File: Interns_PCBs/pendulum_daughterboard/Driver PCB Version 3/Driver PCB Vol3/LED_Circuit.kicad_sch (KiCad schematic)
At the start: 38 parts, among them J4 Conn_01x04, U1 4081, U2 4011, U3 4011, U4 4071

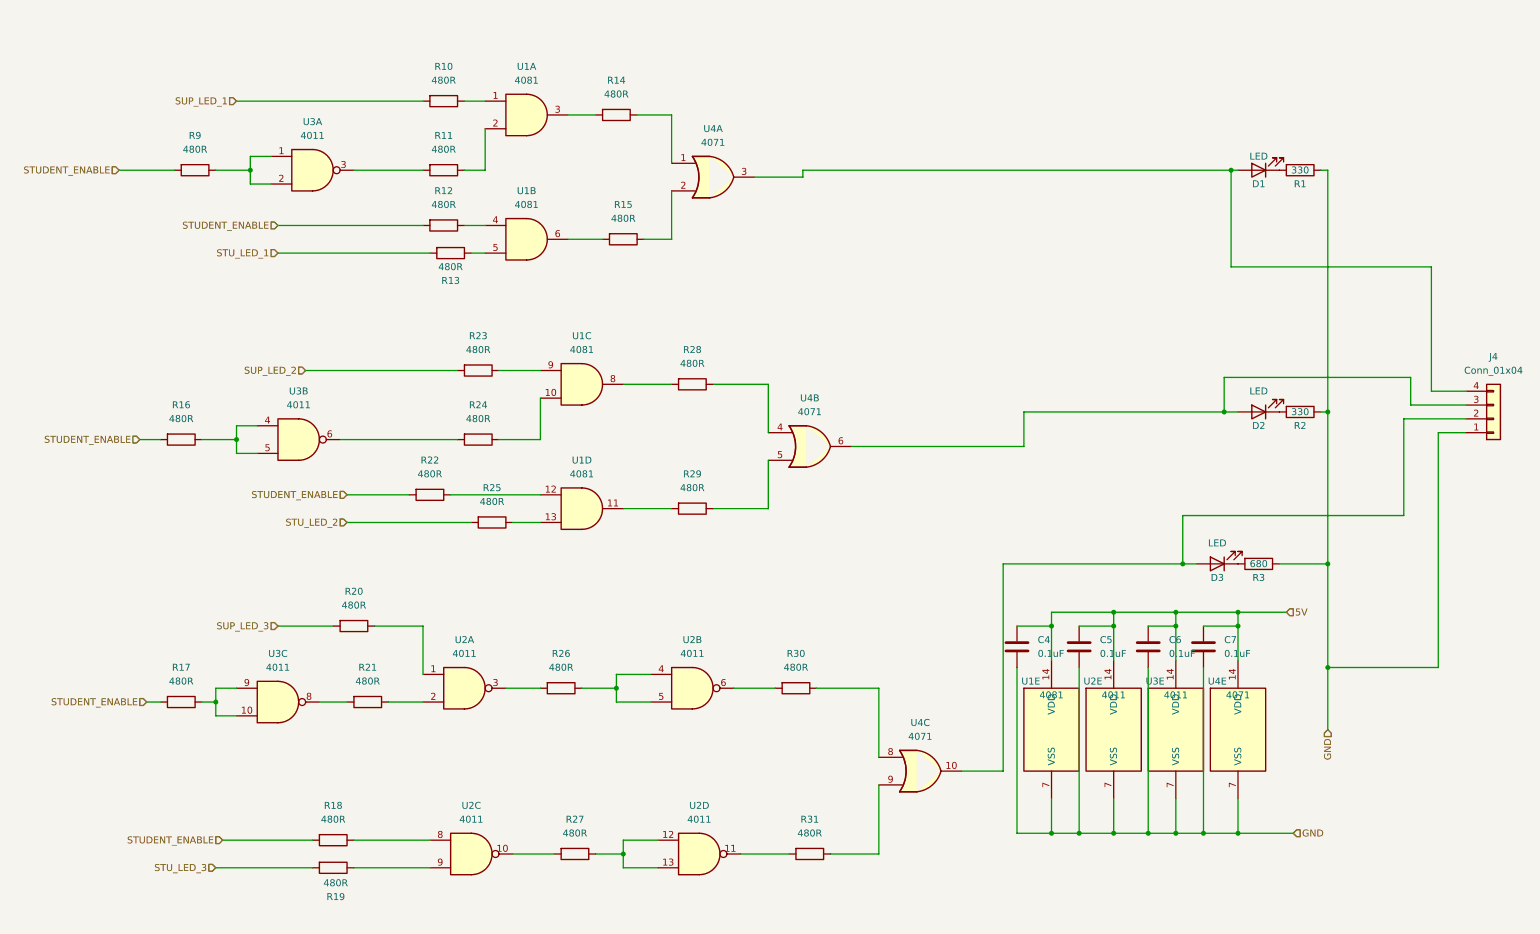
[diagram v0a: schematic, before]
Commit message: Pendulum Driver PCB Vol3
With pull down resistors
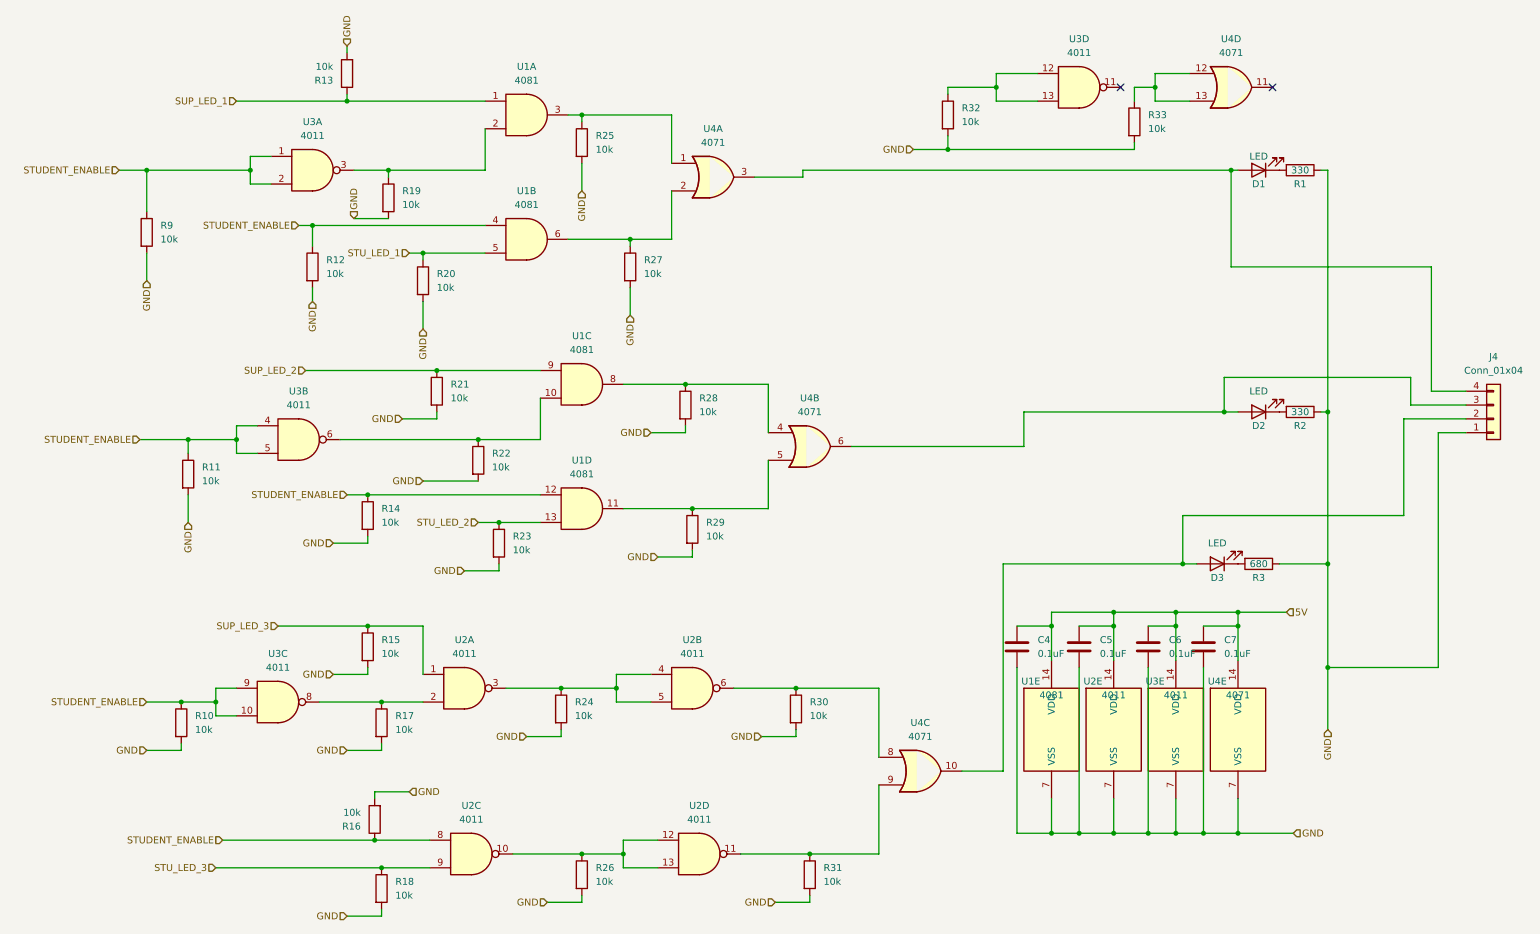
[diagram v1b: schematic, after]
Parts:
- added R32, R33: 10k, Resistor_SMD:R_0805_2012Metric_Pad1.20x1.40mm_HandSolder, symbol Device:R
- added unit 4 of U3
- added unit 4 of U4
- R10, R11, R12, R13, R14, R15, R16, R17, R18, R19, R20, R21, R22, R23, R24, R25, R26, R27, R28, R29, R30, R31, R9: value 480R -> 10k
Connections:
- net GND: now also R10.2, R11.2, R12.2, R13.2, R14.2, R15.2, R16.2, R17.2, R18.2, R19.2, R20.2, R21.2, R22.2, R23.2, R24.2, R25.2, R26.2, R27.2, R28.2, R29.2, R30.2, R31.2, R9.2, R32.2, R33.2
- net STUDENT_ENABLE: now also R10.1, R11.1, R12.1, R14.1, R16.1, R9.1, U1.12, U1.4, U2.8, U3.1, U3.10, U3.2, U3.4, U3.5, U3.9; no longer R12.2, R16.2, R17.2, R18.2, R22.2, R9.2
- net STU_LED_1: now also R20.1, U1.5; no longer R13.2
- net STU_LED_2: now also R23.1, U1.13; no longer R25.2
- net STU_LED_3: now also R18.1, U2.9; no longer R19.2
- net SUP_LED_1: now also R13.1, U1.1; no longer R10.2
- net SUP_LED_2: now also R21.1, U1.9; no longer R23.2
- net SUP_LED_3: now also R15.1, U2.1; no longer R20.2
- net at R22.1: now also U1.10, U3.6; no longer U1.12
- net at U1.2: now also R19.1, U3.3; no longer R11.1
- net at U1.3: now also R25.1, U4.1; no longer R14.2
- net at U2.12, U2.13: now also R26.1, U2.10; no longer R27.1
- net at U2.4, U2.5: now also R24.1, U2.3; no longer R26.1
- net at U2.6: now also R30.1, U4.8; no longer R30.2
- net at R31.1, U4.9: now also U2.11
- net at R28.1, U4.4: now also U1.8
- net at R29.1, U4.5: now also U1.11
- net at U3.8: now also R17.1, U2.2; no longer R21.2
- net at U1.6: now also R27.1, U4.2; no longer R15.2
- new net: R33.1, U4.12, U4.13
- new net: R32.1, U3.12, U3.13
- no-connect marks 0 -> 2
